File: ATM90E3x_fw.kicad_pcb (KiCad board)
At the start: 2 copper layers, 50.8 x 50.8 mm, 67 parts, among them IC1 ATM90E36_ATM90E36, J1 RJ45, J2 CONN_01X04, J3 GS3, J4 GS3, J5 GS3, J6 CONN_01X06, J7 CONN_01X06, J8 CONN_01X04, J9 GROVE-SMD-90D, U1 ROF-78E, Y1 Crystal_GND24

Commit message: Changes from freelancer on fiverr
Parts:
- added C30: 1u/16V, Capacitors_SMD:C_0603, F.Cu at (112.2, 85.2)
- added C31: 100u/16V, Capacitors_SMD:CP_Elec_5x5.8, F.Cu at (143.0, 80.5)
- added C32: 1u/50V, Capacitors_SMD:C_0603, F.Cu at (123.3, 73.6)
- added C33: 220u/50V, Capacitors_SMD:CP_Elec_8x10, F.Cu at (121.4, 79.8)
- added D40: LED, LEDs:LED_0603, F.Cu at (112.1, 80.8)
- added D41: D_Schottky, Diodes_SMD:D_SOD-123, F.Cu at (115.1, 85.2)
- added D42: D_Schottky, Diodes_SMD:D_SOD-123, B.Cu at (132.1, 82.4)
- added D43: D_Schottky, Diodes_SMD:D_SOD-123, B.Cu at (132.1, 79.6)
- added D44: D_Schottky, Diodes_SMD:D_SOD-123, B.Cu at (132.2, 76.5)
- added J10: CONN_01X06, Connectors_JST:JST_SH_SM06B-SRSS-TB_06x1.00mm_Angled, F.Cu at (151.5, 44.9)
- added JP1: Jumper_NC_Small, Connectors:GS2, F.Cu at (123.2, 87.2)
- added R100: R, Resistors_SMD:R_0603_HandSoldering, F.Cu at (113.7, 77.4)
- C3, C7: moved to F.Cu
- D1, IC1, J6, R28, R7, Y1: moved to B.Cu
- moved R12 60.3 mm to (145.7, 59.4), turned to 0 degrees
- moved R16 60.3 mm to (143.6, 66.4)
- moved C2 60.0 mm to (146.9, 63.5), turned to 90 degrees
- moved R23 59.6 mm to (129.9, 63.6), turned to 270 degrees
- moved R13 59.4 mm to (145.5, 63.5), turned to 270 degrees
- moved C1 58.8 mm to (145.7, 60.8), turned to 0 degrees
- moved R19 58.5 mm to (130.8, 66.1), turned to 0 degrees
- moved R10 58.2 mm to (139.7, 66.5)
- moved R21 57.4 mm to (142.4, 63.5), turned to 270 degrees
- moved R20 56.8 mm to (143.9, 63.5), turned to 270 degrees
- moved R11 56.8 mm to (137.3, 66.1), turned to 180 degrees
- moved R15 56.7 mm to (137.7, 63.6), turned to 270 degrees
- moved C10 56.3 mm to (131.5, 63.7)
- moved R22 56.2 mm to (134.7, 63.6), turned to 270 degrees
- moved C9 55.4 mm to (133.1, 63.6), turned to 270 degrees
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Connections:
- MS1 pad 26: Net-(MS1-Pad26) -> USB
- U1 pad 2: Net-(U1-Pad2) -> GND
- U1 pad 3: Net-(MS1-Pad26) -> Net-(C30-Pad1)
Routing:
- net GND: track 0.00 -> 333.4 mm, vias 0 -> 8
- net CS: track 0.00 -> 168.3 mm, vias 0 -> 4
- net SCLK: track 0.00 -> 160.4 mm, vias 0 -> 6
- net MISO: track 0.00 -> 158.7 mm, vias 0 -> 2
- net MOSI: track 0.00 -> 140.2 mm, vias 0 -> 4
- net +3V3: track 0.00 -> 116.8 mm, vias 0 -> 8
- net UB: track 0.00 -> 98.1 mm, vias 0 -> 2
- net UA: track 0.00 -> 95.9 mm, vias 0 -> 2
- net UC: track 0.00 -> 90.3 mm
- net I1P_IN: track 0.00 -> 42.6 mm, vias 0 -> 1
- net Net-(C30-Pad1): track 0.00 -> 40.8 mm
- net I1N_IN: track 0.00 -> 37.0 mm, vias 0 -> 1
- net I2P_IN: track 0.00 -> 35.7 mm, vias 0 -> 1
- net I2N_IN: track 0.00 -> 32.8 mm, vias 0 -> 1
- net I3P_IN: track 0.00 -> 31.5 mm, vias 0 -> 1
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
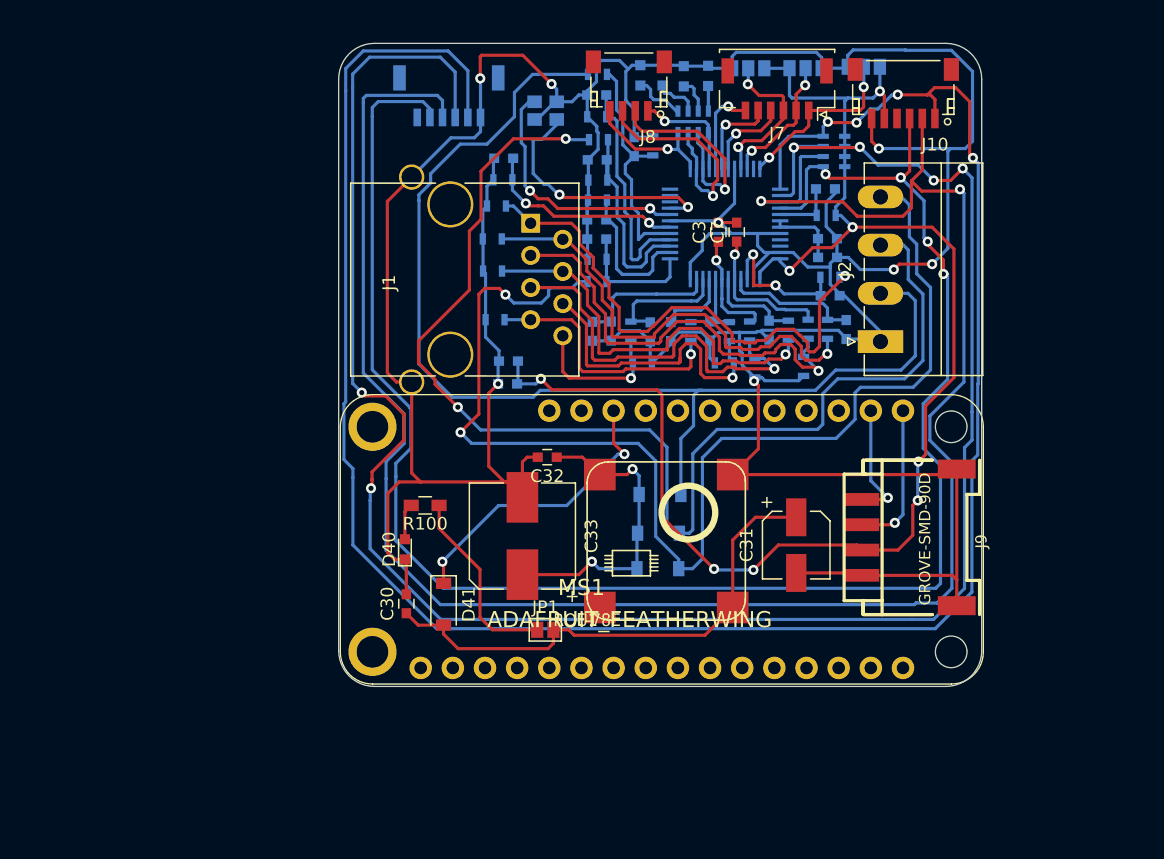
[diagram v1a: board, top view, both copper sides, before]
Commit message: Updates from urbito, wired up featherwing
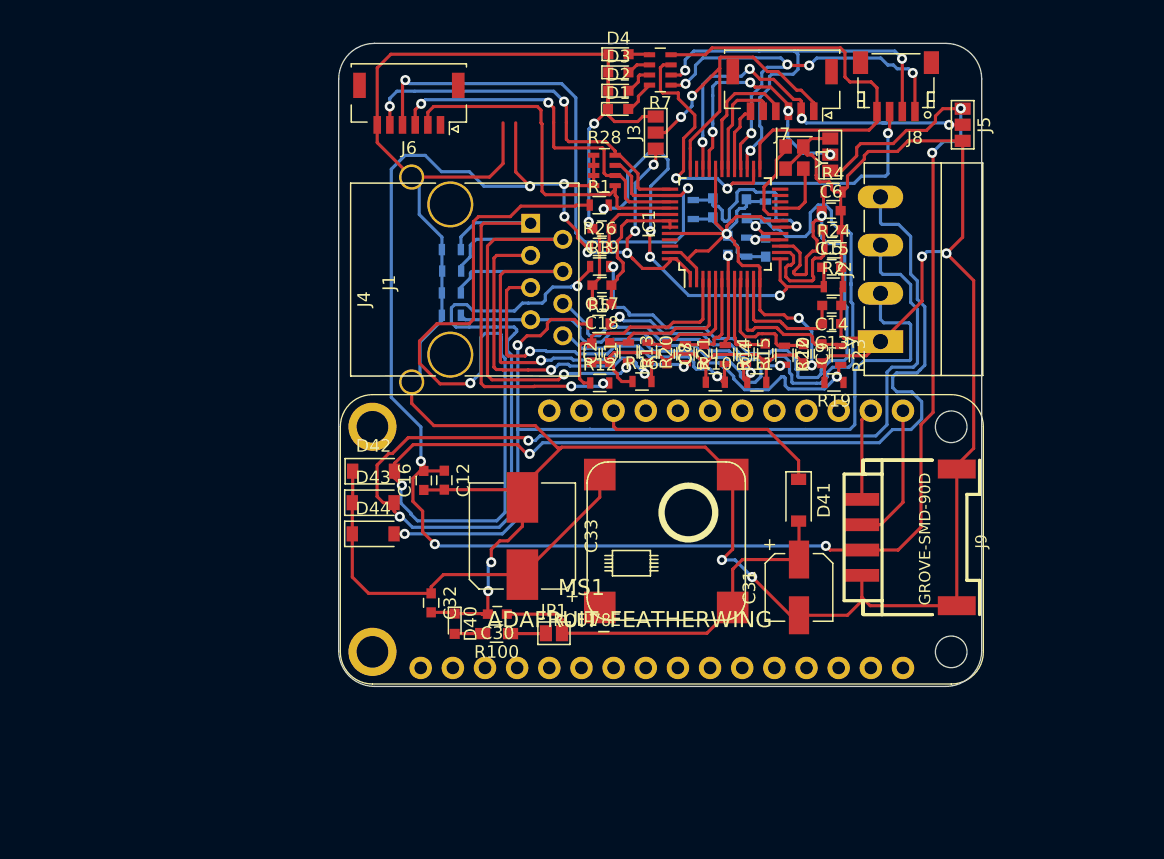
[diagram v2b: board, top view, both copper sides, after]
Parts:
- removed J10: CONN_01X06, Connectors_JST:JST_SH_SM06B-SRSS-TB_06x1.00mm_Angled
- removed LOGO1: OPEN_HARDWARE_1, Symbols:OSHW-Logo2_7.3x6mm_SilkScreen
- C1, C10, C12, C13, C14, C15, C16, C17, C18, C19, C2, C4, C5, C6, C8, C9, D1, D2, D3, D4, D42, D43, D44, IC1, J3, J4, J5, J6, R1, R10, R11, R12, R13, R14, R15, R16, R19, R2, R20, R21, R22, R23, R24, R26, R28, R3, R4, R5, R7, Y1: moved to F.Cu
- C3: moved to B.Cu
- moved D41 29.2 mm to (143.2, 77.0)
- moved D42 23.7 mm to (109.6, 74.7)
- moved D44 22.9 mm to (109.6, 79.6)
- moved D43 22.7 mm to (109.6, 77.2)
- moved J8 21.1 mm to (150.9, 44.3)
- moved R12 20.0 mm to (127.5, 67.7)
- moved Y1 20.0 mm to (142.9, 49.9), turned to 270 degrees
- moved R5 19.7 mm to (127.4, 63.0)
- moved C1 19.4 mm to (126.8, 65.3), turned to 270 degrees
- moved R24 19.1 mm to (146.0, 57.1), turned to 0 degrees
- moved C14 19.0 mm to (145.8, 61.6), turned to 180 degrees
- moved C6 18.9 mm to (145.8, 54.1), turned to 0 degrees
- moved R2 18.8 mm to (145.9, 60.1), turned to 0 degrees
- moved C2 18.8 mm to (128.3, 65.3)
- moved C5 18.7 mm to (145.8, 58.6), turned to 0 degrees
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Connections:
- MS1 pad 2: Net-(MS1-Pad2) -> +3V3
- MS1 pad 4: Net-(MS1-Pad4) -> GND
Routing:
- net CS: track 168.3 -> 30.2 mm, vias 4 -> 2
- net MISO: track 158.7 -> 28.7 mm
- net SCLK: track 160.4 -> 48.9 mm, vias 6 -> 2
- net MOSI: track 140.2 -> 29.0 mm, vias 4 -> 0
- net +3V3: track 116.8 -> 172.6 mm, vias 8 -> 12
- net V2P: track 16.9 -> 51.8 mm, vias 0 -> 2
- net UA: track 95.9 -> 128.6 mm, vias 2 -> 3
- net V3P: track 19.0 -> 49.4 mm, vias 0 -> 2
- net V1P: track 9.98 -> 36.5 mm, vias 0 -> 4
- net CF4: track 8.75 -> 35.1 mm, vias 1 -> 5
- net CF1: track 10.5 -> 33.6 mm, vias 1 -> 0
- net PM1: track 10.6 -> 30.5 mm, vias 2 -> 4
- net CF2: track 18.8 -> 38.0 mm, vias 1 -> 3
- net CF3: track 17.7 -> 36.2 mm, vias 1 -> 3
- net IN_IN: track 11.8 -> 28.1 mm
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
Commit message: Urbito delivery
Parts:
- removed J6: CONN_01X06, Connectors_JST:JST_SHL_SM06B-SHLS-TF_06x1.00mm_Angled
- added J10: CONN_01X06, Connectors_JST:JST_SH_SM06B-SRSS-TB_06x1.00mm_Angled, F.Cu at (146.1, 44.7)
- added LOGO1: OPEN_HARDWARE_1, Symbols:OSHW-Logo2_7.3x6mm_SilkScreen, B.Cu at (135.6, 81.5)
- C1, C10, C13, C15, C17, C19, C2, C4, C5, C6, C7, C8, C9, IC1, J3, J4, J5, JP1: moved to B.Cu
- R25, R27, R6: moved to F.Cu
- moved C12 28.3 mm to (111.8, 47.3)
- moved C16 28.3 mm to (110.3, 47.3)
- moved J8 23.9 mm to (127.0, 44.6)
- moved C14 19.3 mm to (126.9, 65.2), turned to 90 degrees
- moved C18 19.2 mm to (145.8, 55.3), turned to 0 degrees
- moved R4 19.2 mm to (127.6, 58.3), turned to 180 degrees
- moved C13 19.0 mm to (126.9, 65.2), turned to 90 degrees
- moved C17 18.8 mm to (145.8, 55.3), turned to 0 degrees
- moved C15 18.6 mm to (127.7, 59.9), turned to 0 degrees
- moved C6 18.6 mm to (127.6, 58.3), turned to 180 degrees
- moved R26 18.5 mm to (145.8, 53.8), turned to 180 degrees
- moved R24 18.4 mm to (127.7, 59.8), turned to 180 degrees
- moved C5 18.3 mm to (127.7, 61.3), turned to 180 degrees
- moved R2 18.3 mm to (127.7, 61.4), turned to 180 degrees
- moved C19 18.2 mm to (145.8, 53.8), turned to 0 degrees
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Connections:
- MS1 pad 2: +3V3 -> Net-(MS1-Pad2)
- MS1 pad 4: GND -> Net-(MS1-Pad4)
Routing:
- net GND: track 345.9 -> 40.2 mm, vias 11 -> 33
- net +3V3: track 172.6 -> 123.0 mm, vias 12 -> 4
- net V2P: track 51.8 -> 7.03 mm, vias 2 -> 1
- net SCLK: track 48.9 -> 6.09 mm, vias 2 -> 1
- net UA: track 128.6 -> 88.5 mm, vias 3 -> 5
- net V3P: track 49.4 -> 9.87 mm
- net UB: track 109.9 -> 78.0 mm, vias 3 -> 5
- net V1P: track 36.5 -> 9.13 mm, vias 4 -> 1
- net IN_IN: track 28.1 -> 7.48 mm, vias 1 -> 0
- net PM1: track 30.5 -> 11.0 mm, vias 4 -> 1
- net CS: track 30.2 -> 11.3 mm
- net CF2: track 38.0 -> 20.1 mm, vias 3 -> 2
- net MISO: track 28.7 -> 11.6 mm, vias 2 -> 1
- net CF3: track 36.2 -> 19.2 mm, vias 3 -> 1
- net DMA: track 27.2 -> 11.0 mm, vias 2 -> 1
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- added copper zone on B.Cu, net GND
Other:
- net class +3v3 added: clearance 0.2, trace_width 0.3, via_dia 0.8, via_drill 0.4
- net class Default: clearance 0.2 -> 0.1; trace_width 0.25 -> 0.3; via_dia 0.8 -> 0.5
- net class GND added: clearance 0.2, trace_width 0.3, via_dia 0.8, via_drill 0.4
- net class VCC added: clearance 0.2, trace_width 0.3, via_dia 0.8, via_drill 0.4
- rule trace_clearance: 0.2 -> 0.1

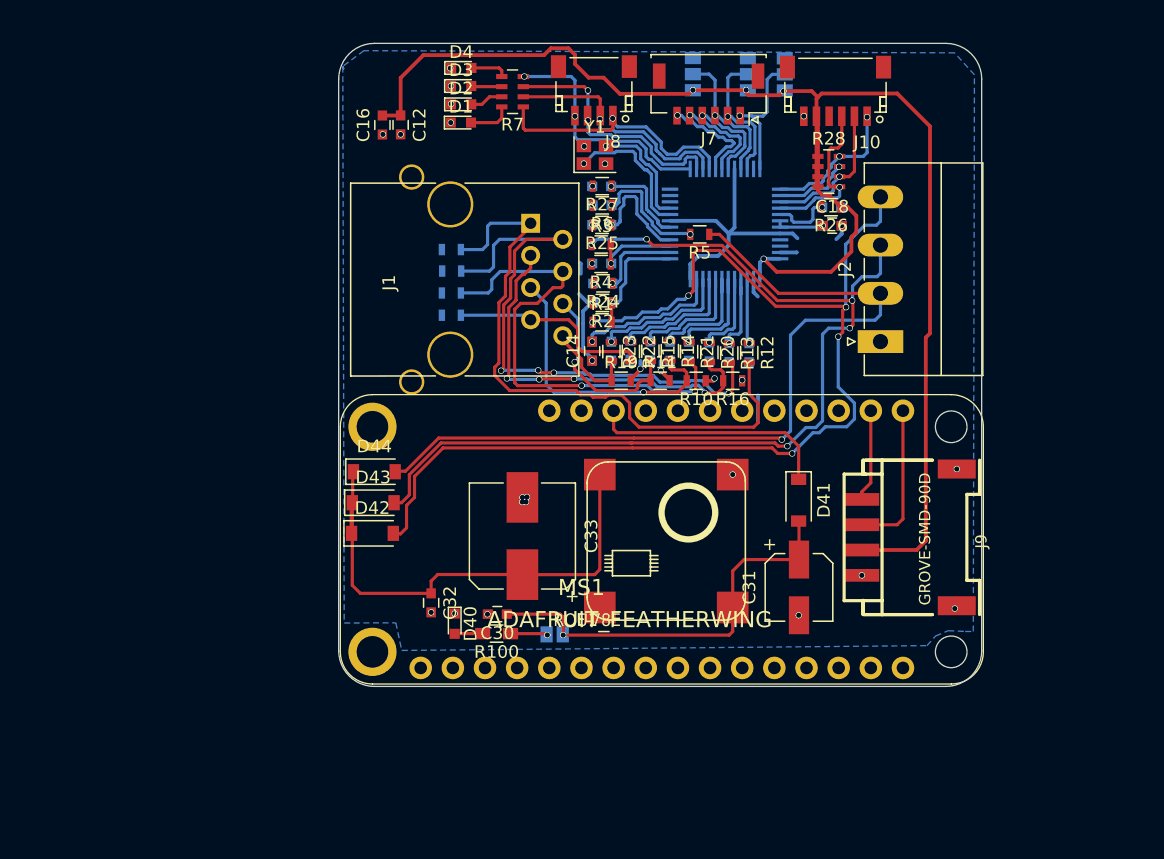
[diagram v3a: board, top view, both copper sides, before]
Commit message: Urbito delivery gnd plane fix
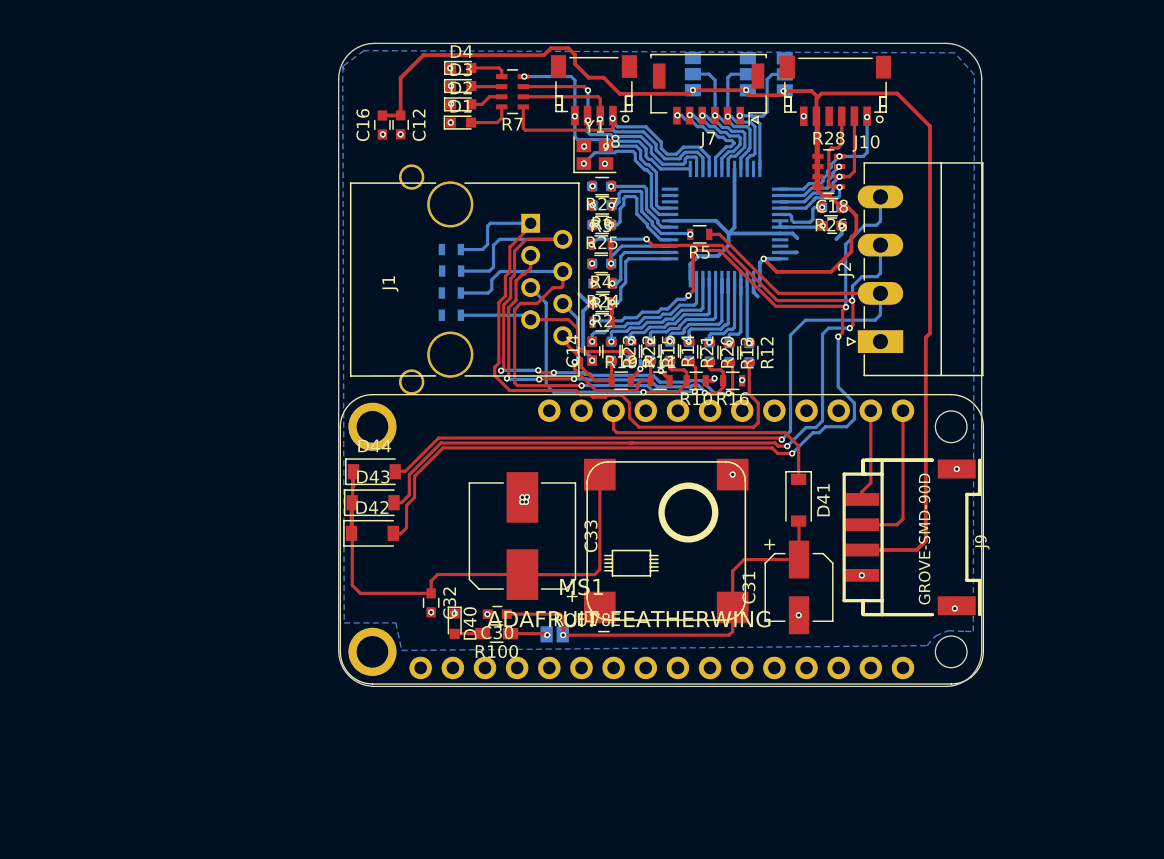
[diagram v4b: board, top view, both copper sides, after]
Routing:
- net (no net): track 2.99 -> 0.00 mm
- net Net-(C32-Pad1): track 40.1 -> 41.4 mm
- net V1P: track 9.13 -> 9.90 mm
